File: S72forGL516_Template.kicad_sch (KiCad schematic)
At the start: 235 parts, among them J1 Conn_01x02, J10 Conn_01x01, J11 Conn_01x01, J12 Conn_01x01, J13 Conn_01x01, J14 Conn_01x01, J15 Conn_01x01, J16 Conn_01x01, J17 Conn_01x01, J2 Conn_01x01, J3 Conn_01x01, J4 Conn_01x01, J5 Conn_01x01, J6 Conn_01x01, J7 Conn_01x01, J8 Conn_01x01, J9 Conn_01x01, SW1 RotaryEncoder_Switch, SW10 SW_PUSH, SW11 SW_PUSH, SW12 SW_PUSH, SW13 SW_PUSH, SW14 SW_PUSH, SW15 SW_PUSH, SW16 SW_PUSH, SW17 SW_PUSH, SW18 SW_PUSH, SW19 SW_PUSH, SW2 SW_PUSH, SW20 SW_PUSH, SW21 SW_PUSH, SW22 SW_PUSH, SW23 SW_PUSH, SW24 SW_PUSH, SW25 SW_PUSH, SW26 SW_PUSH, SW27 SW_PUSH, SW28 SW_PUSH, SW29 SW_PUSH, SW3 SW_PUSH, SW30 SW_PUSH, SW31 SW_PUSH, SW32 SW_PUSH, SW33 SW_PUSH, SW34 SW_PUSH, SW35 SW_PUSH, SW36 SW_PUSH, SW37 SW_PUSH, SW38 SW_PUSH, SW39 SW_PUSH, SW4 SW_PUSH, SW40 SW_PUSH, SW41 SW_PUSH, SW42 SW_PUSH, SW43 SW_PUSH, SW44 SW_PUSH, SW45 SW_PUSH, SW46 SW_PUSH, SW47 SW_PUSH, SW48 SW_PUSH, SW49 SW_PUSH, SW5 SW_PUSH, SW50 SW_PUSH, SW51 SW_PUSH, SW52 SW_PUSH, SW53 SW_PUSH, SW54 SW_PUSH, SW55 SW_PUSH, SW56 SW_PUSH, SW57 SW_PUSH, SW58 SW_PUSH, SW59 SW_PUSH, SW6 SW_PUSH, SW60 SW_PUSH, SW61 SW_PUSH, SW62 SW_PUSH, SW63 SW_PUSH, SW64 SW_PUSH, SW65 SW_PUSH, SW66 SW_PUSH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

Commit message: フットプリントを紐づけ
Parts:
- SW1: footprint (none) -> kbd_Parts:RotaryEncoder_EC12E
- SW18, SW70, SW71: footprint kbd_SW:CherryMX_Hotswap_1u -> kbd_SW:CherryMX_Hotswap_1.5u
- SW31: footprint kbd_SW:CherryMX_Hotswap_1u -> kbd_SW:CherryMX_Hotswap_ISO_Rev
- SW33, SW59: footprint kbd_SW:CherryMX_Hotswap_1u -> kbd_SW:CherryMX_Hotswap_1.75u
- SW47: footprint kbd_SW:CherryMX_Hotswap_1u -> kbd_SW:CherryMX_Hotswap_2.25u_Rev
- SW61, SW62, SW63, SW69: footprint kbd_SW:CherryMX_Hotswap_1u -> kbd_SW:CherryMX_Hotswap_1.25u
- SW68: footprint kbd_SW:CherryMX_Hotswap_1u -> kbd_SW:CherryMX_Hotswap_2u_Rev
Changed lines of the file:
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@@
     (property "Reference" "SW18" (id 0) (at 64.77 60.833 0))
     (property "Value" "SW_PUSH" (id 1) (at 64.77 63.1444 0))
-    (property "Footprint" "kbd_SW:CherryMX_Hotswap_1u" (id 2) (at 64.77 67.31 0)
+    (property "Footprint" "kbd_SW:CherryMX_Hotswap_1.5u" (id 2) (at 64.77 67.31 0)
       (effects (font (size 1.27 1.27)) hide)
     )
@@
     (property "Reference" "SW33" (id 0) (at 64.77 79.883 0))
     (property "Value" "SW_PUSH" (id 1) (at 64.77 82.1944 0))
-    (property "Footprint" "kbd_SW:CherryMX_Hotswap_1u" (id 2) (at 64.77 86.36 0)
+    (property "Footprint" "kbd_SW:CherryMX_Hotswap_1.75u" (id 2) (at 64.77 86.36 0)
       (effects (font (size 1.27 1.27)) hide)
     )
@@
     (property "Reference" "SW47" (id 0) (at 64.77 97.663 0))
     (property "Value" "SW_PUSH" (id 1) (at 64.77 99.9744 0))
-    (property "Footprint" "kbd_SW:CherryMX_Hotswap_1u" (id 2) (at 64.77 104.14 0)
+    (property "Footprint" "kbd_SW:CherryMX_Hotswap_2.25u_Rev" (id 2) (at 64.77 104.14 0)
       (effects (font (size 1.27 1.27)) hide)
     )
@@
     (property "Reference" "SW61" (id 0) (at 64.77 114.808 0))
     (property "Value" "SW_PUSH" (id 1) (at 64.77 117.1194 0))
-    (property "Footprint" "kbd_SW:CherryMX_Hotswap_1u" (id 2) (at 64.77 121.285 0)
+    (property "Footprint" "kbd_SW:CherryMX_Hotswap_1.25u" (id 2) (at 64.77 121.285 0)
       (effects (font (size 1.27 1.27)) hide)
     )
@@
     (property "Reference" "SW62" (id 0) (at 81.28 114.808 0))
     (property "Value" "SW_PUSH" (id 1) (at 81.28 117.1194 0))
-    (property "Footprint" "kbd_SW:CherryMX_Hotswap_1u" (id 2) (at 81.28 121.285 0)
+    (property "Footprint" "kbd_SW:CherryMX_Hotswap_1.25u" (id 2) (at 81.28 121.285 0)
       (effects (font (size 1.27 1.27)) hide)
     )
@@
     (property "Reference" "SW63" (id 0) (at 97.79 114.808 0))
     (property "Value" "SW_PUSH" (id 1) (at 97.79 117.1194 0))
-    (property "Footprint" "kbd_SW:CherryMX_Hotswap_1u" (id 2) (at 97.79 121.285 0)
+    (property "Footprint" "kbd_SW:CherryMX_Hotswap_1.25u" (id 2) (at 97.79 121.285 0)
       (effects (font (size 1.27 1.27)) hide)
     )
@@
     (property "Reference" "SW71" (id 0) (at 281.305 114.808 0))
     (property "Value" "SW_PUSH" (id 1) (at 281.305 117.1194 0))
-    (property "Footprint" "kbd_SW:CherryMX_Hotswap_1u" (id 2) (at 281.305 121.285 0)
+    (property "Footprint" "kbd_SW:CherryMX_Hotswap_1.5u" (id 2) (at 281.305 121.285 0)
       (effects (font (size 1.27 1.27)) hide)
     )
@@
     (property "Reference" "SW70" (id 0) (at 264.795 114.808 0))
     (property "Value" "SW_PUSH" (id 1) (at 264.795 117.1194 0))
-    (property "Footprint" "kbd_SW:CherryMX_Hotswap_1u" (id 2) (at 264.795 121.285 0)
+    (property "Footprint" "kbd_SW:CherryMX_Hotswap_1.5u" (id 2) (at 264.795 121.285 0)
       (effects (font (size 1.27 1.27)) hide)
     )
@@
     (property "Reference" "SW69" (id 0) (at 248.285 114.808 0))
     (property "Value" "SW_PUSH" (id 1) (at 248.285 117.1194 0))
-    (property "Footprint" "kbd_SW:CherryMX_Hotswap_1u" (id 2) (at 248.285 121.285 0)
+    (property "Footprint" "kbd_SW:CherryMX_Hotswap_1.25u" (id 2) (at 248.285 121.285 0)
       (effects (font (size 1.27 1.27)) hide)
     )
@@
     (property "Reference" "SW68" (id 0) (at 215.265 114.808 0))
     (property "Value" "SW_PUSH" (id 1) (at 215.265 117.1194 0))
-    (property "Footprint" "kbd_SW:CherryMX_Hotswap_1u" (id 2) (at 215.265 121.285 0)
+    (property "Footprint" "kbd_SW:CherryMX_Hotswap_2u_Rev" (id 2) (at 215.265 121.285 0)
       (effects (font (size 1.27 1.27)) hide)
     )
@@
     (property "Reference" "SW59" (id 0) (at 297.815 97.663 0))
     (property "Value" "SW_PUSH" (id 1) (at 297.815 99.9744 0))
-    (property "Footprint" "kbd_SW:CherryMX_Hotswap_1u" (id 2) (at 297.815 104.14 0)
+    (property "Footprint" "kbd_SW:CherryMX_Hotswap_1.75u" (id 2) (at 297.815 104.14 0)
       (effects (font (size 1.27 1.27)) hide)
     )
@@
     (property "Reference" "SW31" (id 0) (at 297.815 60.833 0))
     (property "Value" "SW_PUSH" (id 1) (at 297.815 63.1444 0))
-    (property "Footprint" "kbd_SW:CherryMX_Hotswap_1u" (id 2) (at 297.815 67.31 0)
+    (property "Footprint" "kbd_SW:CherryMX_Hotswap_ISO_Rev" (id 2) (at 297.815 67.31 0)
       (effects (font (size 1.27 1.27)) hide)
     )
@@
       (effects (font (size 1.27 1.27)) (justify left))
     )
-    (property "Footprint" "" (id 2) (at 52.324 36.83 0)
+    (property "Footprint" "kbd_Parts:RotaryEncoder_EC12E" (id 2) (at 52.324 36.83 0)
       (effects (font (size 1.27 1.27)) hide)
     )
@@
     )
     (path "/ca9033d0-196e-4bb1-b3b5-889086383ed0"
-      (reference "SW1") (unit 1) (value "RotaryEncoder_Switch") (footprint "")
+      (reference "SW1") (unit 1) (value "RotaryEncoder_Switch") (footprint "kbd_Parts:RotaryEncoder_EC12E")
     )
     (path "/00000000-0000-0000-0000-00005bf16d93"
@@
     )
     (path "/00000000-0000-0000-0000-00005bf16f8b"
-      (reference "SW18") (unit 1) (value "SW_PUSH") (footprint "kbd_SW:CherryMX_Hotswap_1u")
+      (reference "SW18") (unit 1) (value "SW_PUSH") (footprint "kbd_SW:CherryMX_Hotswap_1.5u")
     )
     (path "/00000000-0000-0000-0000-00005c3d9a54"
@@
     )
     (path "/00000000-0000-0000-0000-000060c8f2a4"
-      (reference "SW31") (unit 1) (value "SW_PUSH") (footprint "kbd_SW:CherryMX_Hotswap_1u")
+      (reference "SW31") (unit 1) (value "SW_PUSH") (footprint "kbd_SW:CherryMX_Hotswap_ISO_Rev")
     )
     (path "/00000000-0000-0000-0000-00005c3dce20"
@@
     )
     (path "/00000000-0000-0000-0000-00005c3dcefa"
-      (reference "SW33") (unit 1) (value "SW_PUSH") (footprint "kbd_SW:CherryMX_Hotswap_1u")
+      (reference "SW33") (unit 1) (value "SW_PUSH") (footprint "kbd_SW:CherryMX_Hotswap_1.75u")
     )
     (path "/00000000-0000-0000-0000-00005c3dcfd2"
@@
     )
     (path "/00000000-0000-0000-0000-00005c3dcf5c"
-      (reference "SW47") (unit 1) (value "SW_PUSH") (footprint "kbd_SW:CherryMX_Hotswap_1u")
+      (reference "SW47") (unit 1) (value "SW_PUSH") (footprint "kbd_SW:CherryMX_Hotswap_2.25u_Rev")
     )
     (path "/00000000-0000-0000-0000-00005c3dee7c"
@@
     )
     (path "/00000000-0000-0000-0000-000060c8f28d"
-      (reference "SW59") (unit 1) (value "SW_PUSH") (footprint "kbd_SW:CherryMX_Hotswap_1u")
+      (reference "SW59") (unit 1) (value "SW_PUSH") (footprint "kbd_SW:CherryMX_Hotswap_1.75u")
     )
     (path "/00000000-0000-0000-0000-00005c6ab630"
@@
     )
     (path "/00000000-0000-0000-0000-00005c6ab742"
-      (reference "SW61") (unit 1) (value "SW_PUSH") (footprint "kbd_SW:CherryMX_Hotswap_1u")
+      (reference "SW61") (unit 1) (value "SW_PUSH") (footprint "kbd_SW:CherryMX_Hotswap_1.25u")
     )
     (path "/00000000-0000-0000-0000-00005c6aba0e"
-      (reference "SW62") (unit 1) (value "SW_PUSH") (footprint "kbd_SW:CherryMX_Hotswap_1u")
+      (reference "SW62") (unit 1) (value "SW_PUSH") (footprint "kbd_SW:CherryMX_Hotswap_1.25u")
     )
     (path "/00000000-0000-0000-0000-00005c6abb12"
-      (reference "SW63") (unit 1) (value "SW_PUSH") (footprint "kbd_SW:CherryMX_Hotswap_1u")
+      (reference "SW63") (unit 1) (value "SW_PUSH") (footprint "kbd_SW:CherryMX_Hotswap_1.25u")
     )
     (path "/00000000-0000-0000-0000-00005c6abdea"
@@
     )
     (path "/00000000-0000-0000-0000-000060c8f0d0"
-      (reference "SW68") (unit 1) (value "SW_PUSH") (footprint "kbd_SW:CherryMX_Hotswap_1u")
+      (reference "SW68") (unit 1) (value "SW_PUSH") (footprint "kbd_SW:CherryMX_Hotswap_2u_Rev")
     )
     (path "/00000000-0000-0000-0000-000060c8f0bc"
-      (reference "SW69") (unit 1) (value "SW_PUSH") (footprint "kbd_SW:CherryMX_Hotswap_1u")
+      (reference "SW69") (unit 1) (value "SW_PUSH") (footprint "kbd_SW:CherryMX_Hotswap_1.25u")
     )
     (path "/00000000-0000-0000-0000-000060c8f0b2"
-      (reference "SW70") (unit 1) (value "SW_PUSH") (footprint "kbd_SW:CherryMX_Hotswap_1u")
+      (reference "SW70") (unit 1) (value "SW_PUSH") (footprint "kbd_SW:CherryMX_Hotswap_1.5u")
     )
     (path "/00000000-0000-0000-0000-000060c8f0a8"
-      (reference "SW71") (unit 1) (value "SW_PUSH") (footprint "kbd_SW:CherryMX_Hotswap_1u")
+      (reference "SW71") (unit 1) (value "SW_PUSH") (footprint "kbd_SW:CherryMX_Hotswap_1.5u")
     )
     (path "/00000000-0000-0000-0000-0000612b3e51"

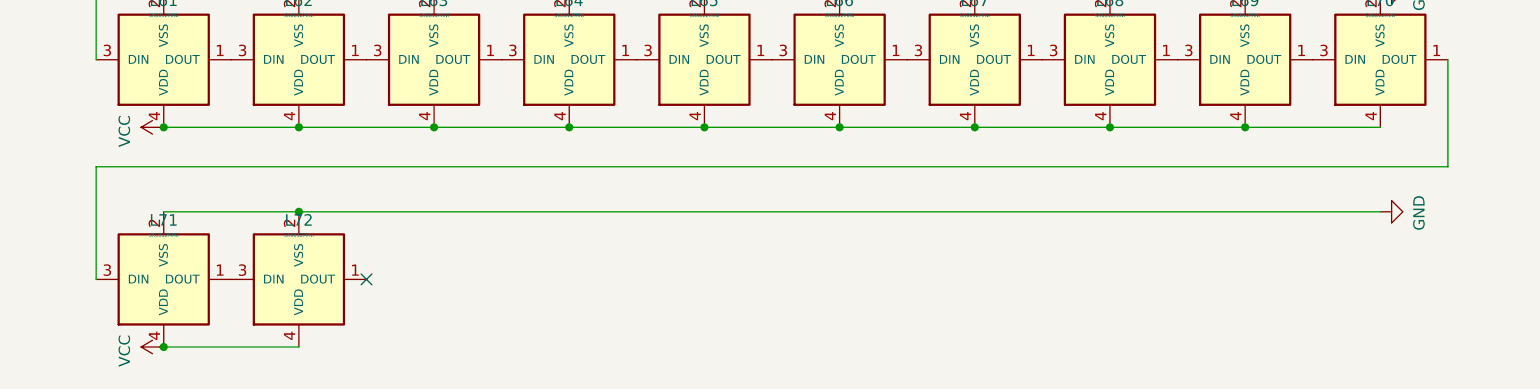
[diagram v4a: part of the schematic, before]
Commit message: フットプリントを配置
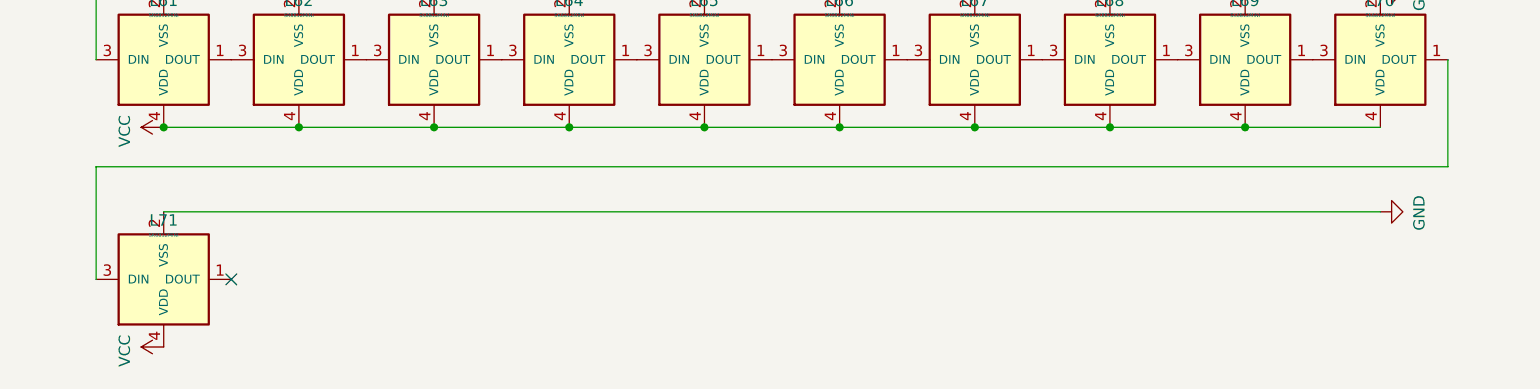
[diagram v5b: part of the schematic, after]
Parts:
- removed L72: SK6812MINI, kbd_Parts:LED_SK6812MINI-E_BL, symbol Salicylic_kbd:LED_SK6812MINI-E
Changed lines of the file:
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@@
   (junction (at 152.4 74.93) (diameter 0) (color 0 0 0 0)
   )
-  (junction (at 58.42 315.595) (diameter 0) (color 0 0 0 0)
-  )
   (junction (at 236.855 111.76) (diameter 0) (color 0 0 0 0)
   )
@@
   (junction (at 119.38 205.74) (diameter 0) (color 0 0 0 0)
   )
-  (junction (at 43.18 330.835) (diameter 0) (color 0 0 0 0)
-  )
   (junction (at 220.345 128.905) (diameter 0) (color 0 0 0 0)
   )
@@
   )
   (no_connect (at 271.78 179.07))
-  (no_connect (at 66.04 323.215))
   (no_connect (at 271.78 207.01))
+  (no_connect (at 50.8 323.215))
   (no_connect (at 236.22 181.61))
   (wire (pts (xy 381 270.51) (xy 381 273.05))
@@
     (stroke (width 0) (type default) (color 0 0 0 0))
   )
-  (wire (pts (xy 43.18 330.835) (xy 58.42 330.835))
-    (stroke (width 0) (type default) (color 0 0 0 0))
-  )
   (wire (pts (xy 119.38 290.83) (xy 134.62 290.83))
     (stroke (width 0) (type default) (color 0 0 0 0))
@@
     (stroke (width 0) (type default) (color 0 0 0 0))
   )
-  (wire (pts (xy 58.42 315.595) (xy 180.34 315.595))
+  (wire (pts (xy 43.18 315.595) (xy 180.34 315.595))
     (stroke (width 0) (type default) (color 0 0 0 0))
   )
@@
     (stroke (width 0) (type default) (color 0 0 0 0))
   )
-  (wire (pts (xy 43.18 315.595) (xy 58.42 315.595))
-    (stroke (width 0) (type default) (color 0 0 0 0))
-  )
   (wire (pts (xy 220.345 74.93) (xy 236.855 74.93))
     (stroke (width 0) (type default) (color 0 0 0 0))
@@
     (pin "1")
   )
-  (symbol (lib_id "Salicylic_kbd:LED_SK6812MINI-E") (at 58.42 323.215 0) (mirror x) (unit 1)
-    (in_bom yes) (on_board yes)
-    (property "Reference" "L72" (id 0) (at 58.42 316.5602 0)
-      (effects (font (size 1.2954 1.2954)))
-    )
-    (property "Value" "SK6812MINI" (id 1) (at 58.42 318.2112 0)
-      (effects (font (size 0.4064 0.4064)))
-    )
-    (property "Footprint" "kbd_Parts:LED_SK6812MINI-E_BL" (id 2) (at 58.42 323.215 0)
-      (effects (font (size 1.524 1.524)) hide)
-    )
-    (property "Datasheet" "" (id 3) (at 58.42 323.215 0)
-      (effects (font (size 1.524 1.524)) hide)
-    )
-    (pin "1")
-    (pin "2")
-    (pin "3")
-    (pin "4")
-  )
   (symbol (lib_id "Salicylic_kbd:LED_SK6812MINI-E") (at 43.18 323.215 0) (mirror x) (unit 1)
     (in_bom yes) (on_board yes)
@@
       (reference "L71") (unit 1) (value "SK6812MINI") (footprint "kbd_Parts:LED_SK6812MINI-E_BL")
     )
-    (path "/00000000-0000-0000-0000-000062e6d56f"
-      (reference "L72") (unit 1) (value "SK6812MINI") (footprint "kbd_Parts:LED_SK6812MINI-E_BL")
-    )
     (path "/ca9033d0-196e-4bb1-b3b5-889086383ed0"
